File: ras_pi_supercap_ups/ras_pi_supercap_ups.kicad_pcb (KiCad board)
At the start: 2 copper layers, 65 x 56 mm, 89 parts, among them J1 Raspberry_Pi_2_3, J10 Conn_01x03, J12 171826-4, J2 Raspberry_Pi_2_3, J3 Conn_01x05, J4 Conn_01x05, J6 Conn_01x04, J7 Conn_01x04, J8 Conn_02x03_Odd_Even, J9 LEDs and Buttons, Q1 IRF5305, U1 KA431AZTA, U10 TPS54331DR, U2 KA431AZTA, U3 KA431AZTA, U4 KA431AZTA, U5 KA431AZTA, U6 LM2596S-5, U7 L7805, U8 ATtiny85-20P, U9 STC8H1K08

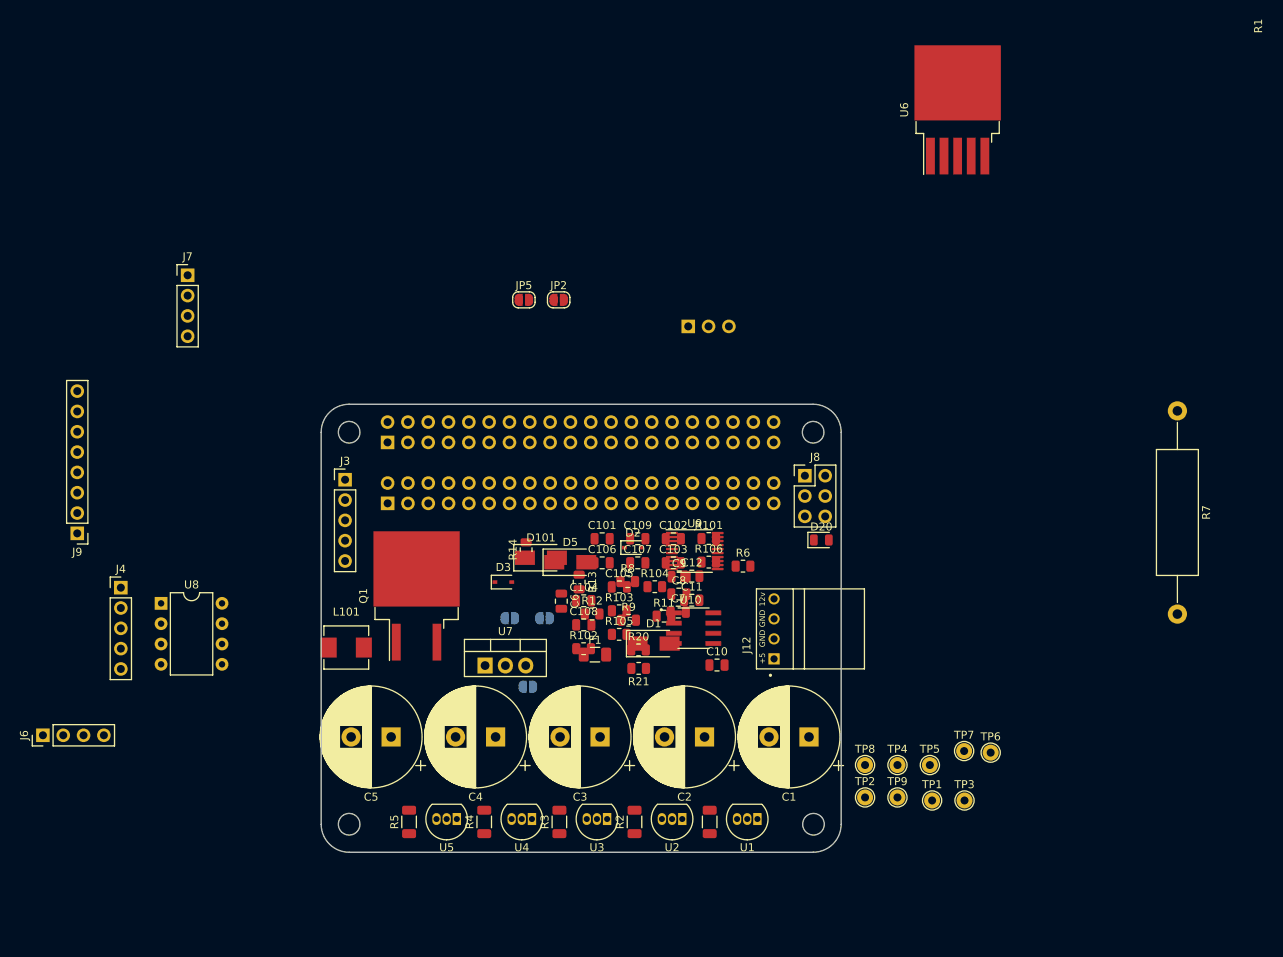
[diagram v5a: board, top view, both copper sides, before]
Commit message: updated layout
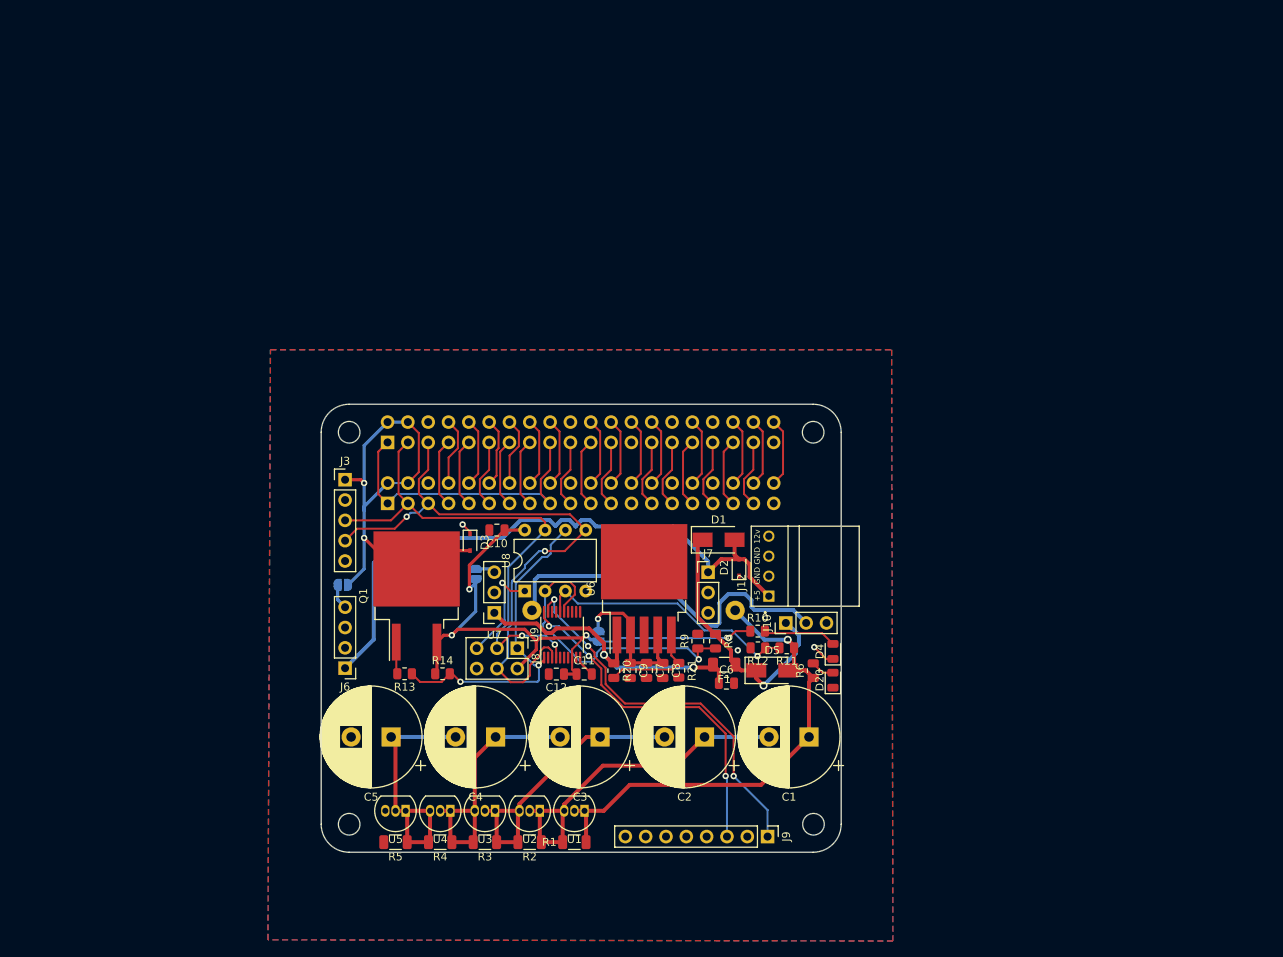
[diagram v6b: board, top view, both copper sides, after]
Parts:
- removed C101, C102: 4.7u, Capacitor_SMD:C_0805_2012Metric
- removed C103, C106: 4.7n, Capacitor_SMD:C_0805_2012Metric
- removed C104: 0.1u, Capacitor_SMD:C_0805_2012Metric
- removed C105: 0.01u, Capacitor_SMD:C_0805_2012Metric
- removed C107: 39p, Capacitor_SMD:C_0805_2012Metric
- removed C108, C109: 33u, Capacitor_SMD:C_0805_2012Metric
- removed D101: B340A, Diode_SMD:D_SMA
- removed J4: Conn_01x05, Connector_PinHeader_2.54mm:PinHeader_1x05_P2.54mm_Vertical
- removed JP4, JP5: SolderJumper_2_Open, Jumper:SolderJumper-2_P1.3mm_Open_RoundedPad1.0x1.5mm
- removed L101: 6.8uH, raspberrypi_supercap_ups_lib:Sunltech_SLO0530H
- removed R101: 332k, Resistor_SMD:R_0805_2012Metric
- removed R102: 68.1k, Resistor_SMD:R_0805_2012Metric
- removed R103: 49.9k, Resistor_SMD:R_0805_2012Metric
- removed R104: 0, Resistor_SMD:R_0805_2012Metric
- removed R105: 10.2k, Resistor_SMD:R_0805_2012Metric
- removed R106: 3.24k, Resistor_SMD:R_0805_2012Metric
- removed TP1, TP2, TP3, TP4, TP5, TP6, TP7, TP8, TP9: TestPoint_Small, TestPoint:TestPoint_THTPad_D2.0mm_Drill1.0mm
- removed U10: TPS54331DR, raspberrypi_supercap_ups_lib:SOIC127P599X175-8N
- added D4: Green, LED_SMD:LED_0805_2012Metric, F.Cu at (114.0, 130.9)
- added R10: 1k, Resistor_SMD:R_0805_2012Metric, F.Cu at (104.6, 128.4)
- J10: moved to F.Cu
- J7: value Conn_01x04 -> Conn_01x03; footprint Connector_PinHeader_2.54mm:PinHeader_1x04_P2.54mm_Vertical -> Connector_PinHeader_2.54mm:PinHeader_1x03_P2.54mm_Vertical
- JP2, R7: moved to B.Cu
- U7: footprint Package_TO_SOT_THT:TO-220-3_Vertical -> Connector_PinSocket_2.54mm:PinSocket_1x03_P2.54mm_Vertical
- moved J9 94.3 mm to (105.8, 154.0), turned to -90 degrees
- moved R7 84.4 mm to (76.3, 125.8), turned to 0 degrees
- moved J7 74.9 mm to (98.4, 121.0)
- moved U6 71.5 mm to (90.4, 123.1)
- moved U8 45.5 mm to (75.5, 123.3), turned to 90 degrees
- moved JP2 42.4 mm to (84.7, 129.0), turned to -90 degrees
- moved J8 41.9 mm to (74.5, 130.5), turned to -90 degrees
- moved J10 39.0 mm to (108.1, 127.3), turned to 90 degrees
- moved J6 38.7 mm to (53.0, 133.0), turned to 180 degrees
- moved C10 32.3 mm to (72.0, 115.7), turned to 180 degrees
- moved D5 28.6 mm to (106.4, 133.3)
- moved JP3 25.6 mm to (52.7, 122.6)
- moved R13 24.7 mm to (60.4, 133.7), turned to 180 degrees
- moved C6 23.0 mm to (100.7, 134.9), turned to 0 degrees
- moved U1 21.6 mm to (82.9, 150.8)
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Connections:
- C7 pad 1: +5V -> Net-(C7-Pad1)
- C8 pad 1: +5V -> Net-(C7-Pad1)
- C9 pad 1: +5V -> Net-(C7-Pad1)
- J7 pad 3: GND -> unconnected-(J7-Pad3)
- JP2 pad 1: /Buck Converter/VIN -> Net-(C7-Pad1)
- JP2 pad 2: Net-(C6-Pad1) -> +5V
- U6 pad 2: +5V -> Net-(C7-Pad1)
- U6 pad 4: +5V -> Net-(C7-Pad1)
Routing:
- net +5V: track 0.00 -> 79.1 mm, vias 0 -> 4
- net VIN: track 0.00 -> 77.3 mm
- net I2C_SDA: track 0.00 -> 77.2 mm, vias 0 -> 2
- net I2C_SCL: track 0.00 -> 63.7 mm, vias 0 -> 2
- net Net-(C1-Pad1): track 0.00 -> 60.8 mm, vias 0 -> 1
- net POW_OUT: track 0.00 -> 59.8 mm, vias 0 -> 2
- net Power_Button: track 0.00 -> 48.1 mm, vias 0 -> 3
- net Net-(J10-Pad2): track 0.00 -> 45.7 mm
- net Net-(C1-Pad2): track 0.00 -> 44.9 mm
- net Spare_Button: track 0.00 -> 43.8 mm, vias 0 -> 3
- net POW_ENABLE: track 0.00 -> 41.7 mm, vias 0 -> 2
- net Net-(C6-Pad1): track 0.00 -> 39.6 mm, vias 0 -> 2
- net VIN_SENSE: track 0.00 -> 39.3 mm, vias 0 -> 1
- net +3V3: track 0.00 -> 38.5 mm
- net Net-(C2-Pad2): track 0.00 -> 37.4 mm
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- added copper zone on B.Cu, net GND
- added copper zone on F.Cu, net GND

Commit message: As ordered v0.9
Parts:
- added J4: Conn_01x03, Connector_PinHeader_2.54mm:PinHeader_1x03_P2.54mm_Vertical, F.Cu at (111.3, 113.0)
- added R15: 1k, Resistor_SMD:R_0805_2012Metric, F.Cu at (98.3, 151.1)
- added R16: 1k, Resistor_SMD:R_0805_2012Metric, F.Cu at (98.3, 149.1)
- added REF**: OSHW-Symbol_6.7x6mm_SilkScreen, Symbol:OSHW-Symbol_6.7x6mm_SilkScreen, F.Cu at (110.7, 119.9)
- added REF**: KiCad-Logo2_5mm_SilkScreen, Symbol:KiCad-Logo2_5mm_SilkScreen, B.Cu at (60.2, 122.4)
- added TP1: TestPoint_Small, TestPoint:TestPoint_THTPad_D1.0mm_Drill0.5mm, F.Cu at (74.9, 147.1)
- J9: footprint Connector_PinHeader_2.54mm:PinHeader_1x08_P2.54mm_Vertical -> Connector_PinHeader_2.54mm:PinHeader_1x04_P2.54mm_Vertical
- U1, U2, U3, U4, U5: value KA431AZTA -> KA431SMFTF; footprint Package_TO_SOT_THT:TO-92_Inline -> Package_TO_SOT_SMD:SOT-23
- U9: footprint Package_SO:TSSOP-20_4.4x5mm_P0.5mm -> Package_SO:TSSOP-20_4.4x6.5mm_P0.65mm
- moved J3 12.9 mm to (53.5, 122.3), turned to 180 degrees
- moved JP2 4.00 mm to (88.2, 130.8), turned to 180 degrees
- moved JP3 3.81 mm to (56.4, 123.6), turned to -90 degrees
- moved U4 1.51 mm to (64.9, 151.6), turned to -90 degrees
- moved U5 1.51 mm to (59.3, 151.6), turned to -90 degrees
- moved U1 1.51 mm to (81.7, 151.6), turned to -90 degrees
- moved U2 1.51 mm to (76.1, 151.6), turned to -90 degrees
- moved U3 1.51 mm to (70.5, 151.6), turned to -90 degrees
- moved U9 0.91 mm to (81.0, 128.8)
- moved J6 0.75 mm to (53.5, 132.4)
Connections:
- J3 pad 3: I2C_SCL -> unconnected-(J3-Pad3)
- J3 pad 4: I2C_SDA -> I2C_SCL
- J3 pad 5: unconnected-(J3-Pad5) -> I2C_SDA
- U1 pad 2: Net-(C1-Pad1) -> Net-(C1-Pad2)
- U1 pad 3: Net-(C1-Pad2) -> Net-(C1-Pad1)
- U2 pad 2: Net-(C1-Pad2) -> Net-(C2-Pad2)
- U2 pad 3: Net-(C2-Pad2) -> Net-(C1-Pad2)
- U3 pad 2: Net-(C2-Pad2) -> Net-(C3-Pad2)
- U3 pad 3: Net-(C3-Pad2) -> Net-(C2-Pad2)
- U4 pad 2: Net-(C3-Pad2) -> Net-(C4-Pad2)
- U4 pad 3: Net-(C4-Pad2) -> Net-(C3-Pad2)
- U5 pad 2: Net-(C4-Pad2) -> GND
- U5 pad 3: GND -> Net-(C4-Pad2)
- U9 pad 9: unconnected-(U9-Pad9) -> Net-(TP1-Pad1)
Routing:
- net RS232_TXD: track 0.00 -> 43.3 mm, vias 0 -> 1
- net RS232_RXD: track 0.00 -> 38.8 mm, vias 0 -> 1
- net +5V: track 79.1 -> 105.9 mm, vias 4 -> 5
- net Net-(TP1-Pad1): track 0.00 -> 18.9 mm
- net GND: track 24.5 -> 32.4 mm, vias 3 -> 22
- net Net-(C1-Pad1): track 60.8 -> 68.6 mm
- net POW_OUT: track 59.8 -> 52.2 mm, vias 2 -> 1
- net Net-(C7-Pad1): track 19.5 -> 13.1 mm
- net Power_Button: track 48.1 -> 52.9 mm, vias 3 -> 4
- net Spare_Button: track 43.8 -> 48.2 mm
- net Net-(C6-Pad1): track 39.6 -> 37.7 mm
- net I2C_SCL: track 63.7 -> 64.9 mm
- net Net-(D1-Pad1): track 33.5 -> 32.4 mm
- net VIN_SENSE: track 39.3 -> 40.2 mm
- net Net-(C4-Pad2): track 32.5 -> 33.4 mm
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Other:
- board text added: "5v"
- board text added: "BAD WOLF"
- board text added: "CHARGE"
- board text added: "DSCHRGE"
- board text added: "GND"
- board text added: "POW EN"
- board text added: "RST"
- board text added: "RXD"
- board text added: "Raspberry Pi 12v UPS v0.9"
- board text added: "SCL"
- board text added: "SDA"
- board text added: "TXD"
- board text added: "VIN"
- board text added: "https://github.com/akuker/hw_projects"
- board text added: "https://github.com/akuker/hw_projects Based upon designs: Scott Baker - 12v SuperCapacitor UPS - http://www.smbaker.com David Gesswein - MFM Emulator - https://www.pdp8online.com/mfm/"
